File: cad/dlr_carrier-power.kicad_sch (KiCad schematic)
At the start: 25 parts, among them J1 PV_IN, J2 BQ24650, J4 LMR33630ADDA, U1 AP2112K-3.3, U2 LP5907MFX-3.8

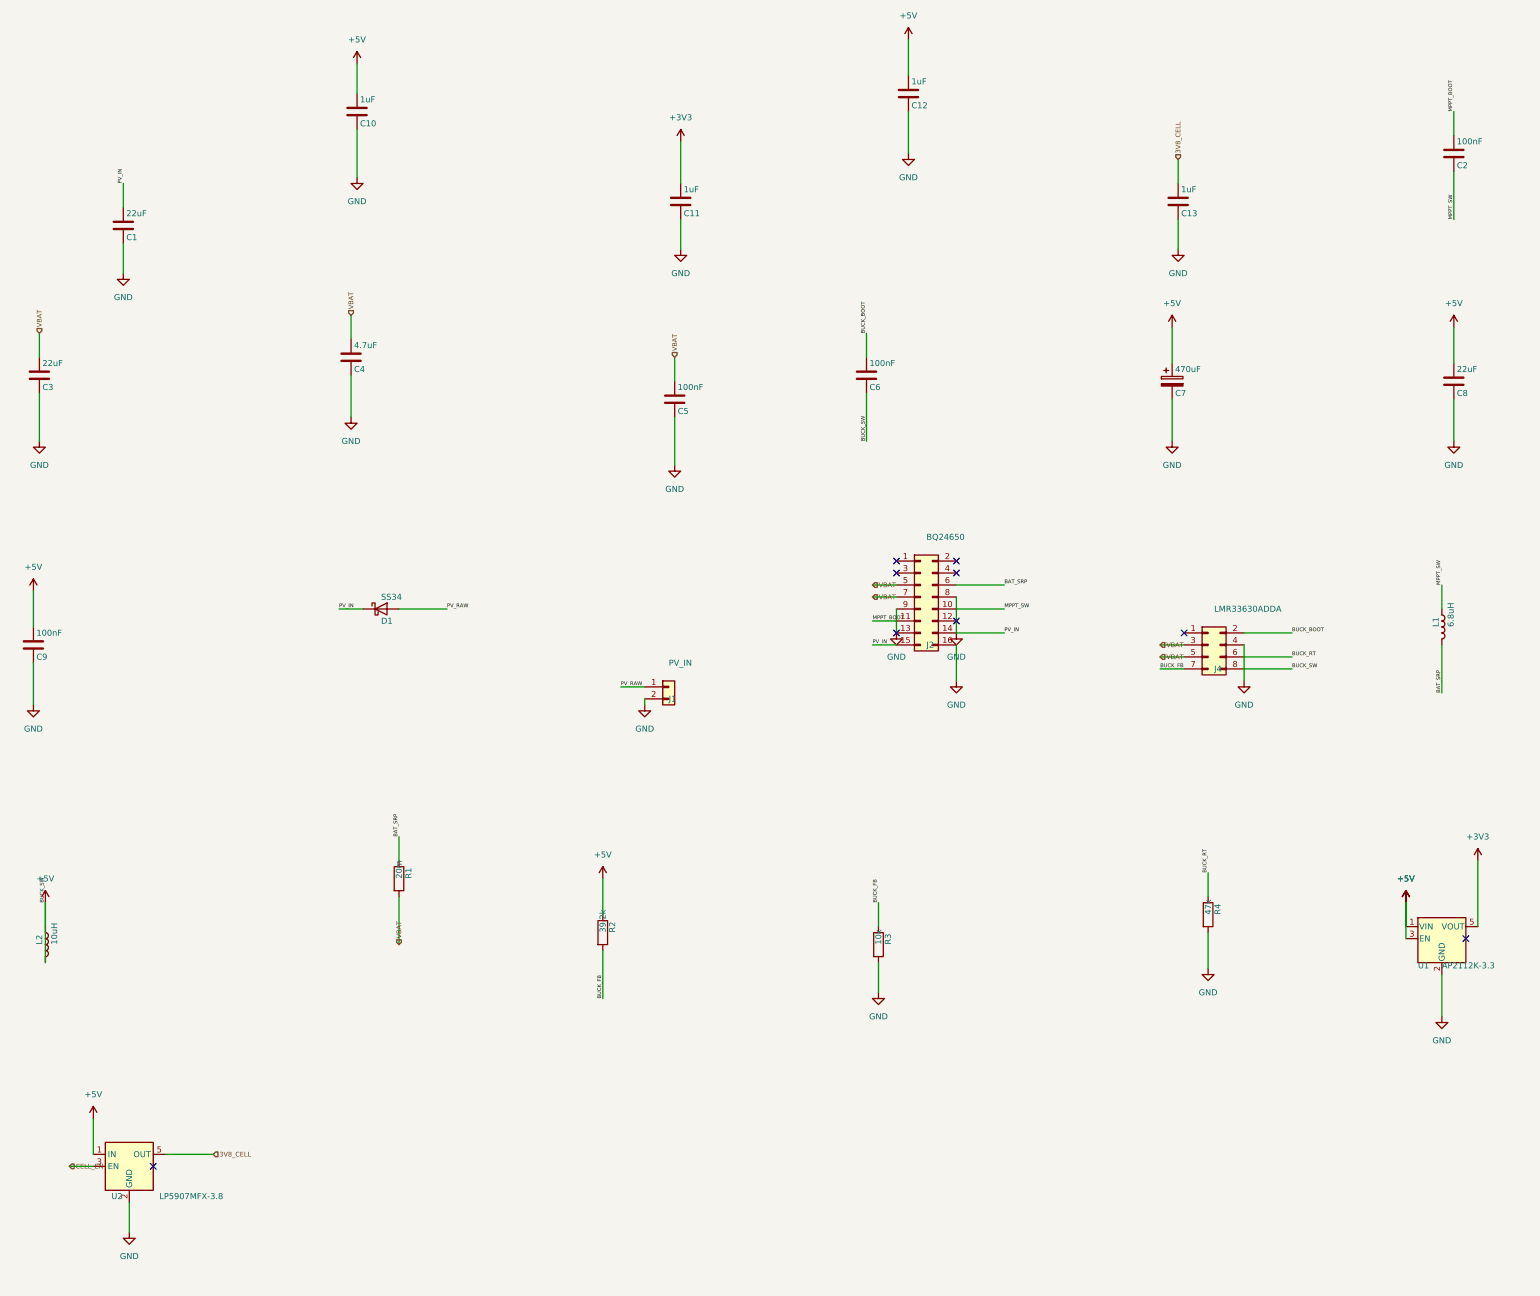
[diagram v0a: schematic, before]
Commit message: 🎨 style: lint fixes (f-string, unused imports, complexity, naming)
CI lint surface from the prior commit:
* F541: drop extraneous `f` prefixes on f-strings without placeholders
* F401: remove unused `math` and `_place_pwr_flags` imports
* C901: extract `_route_sheet_nets` helper so `build_child_sheet`
  complexity drops back under the McCabe threshold
* N806: lowercase local constants in `build_root_sheet`
* black: reformat multi_sheet.py + schematic.py

Co-Authored-By: Claude Opus 4.7 (1M context) <noreply@anthropic.com>
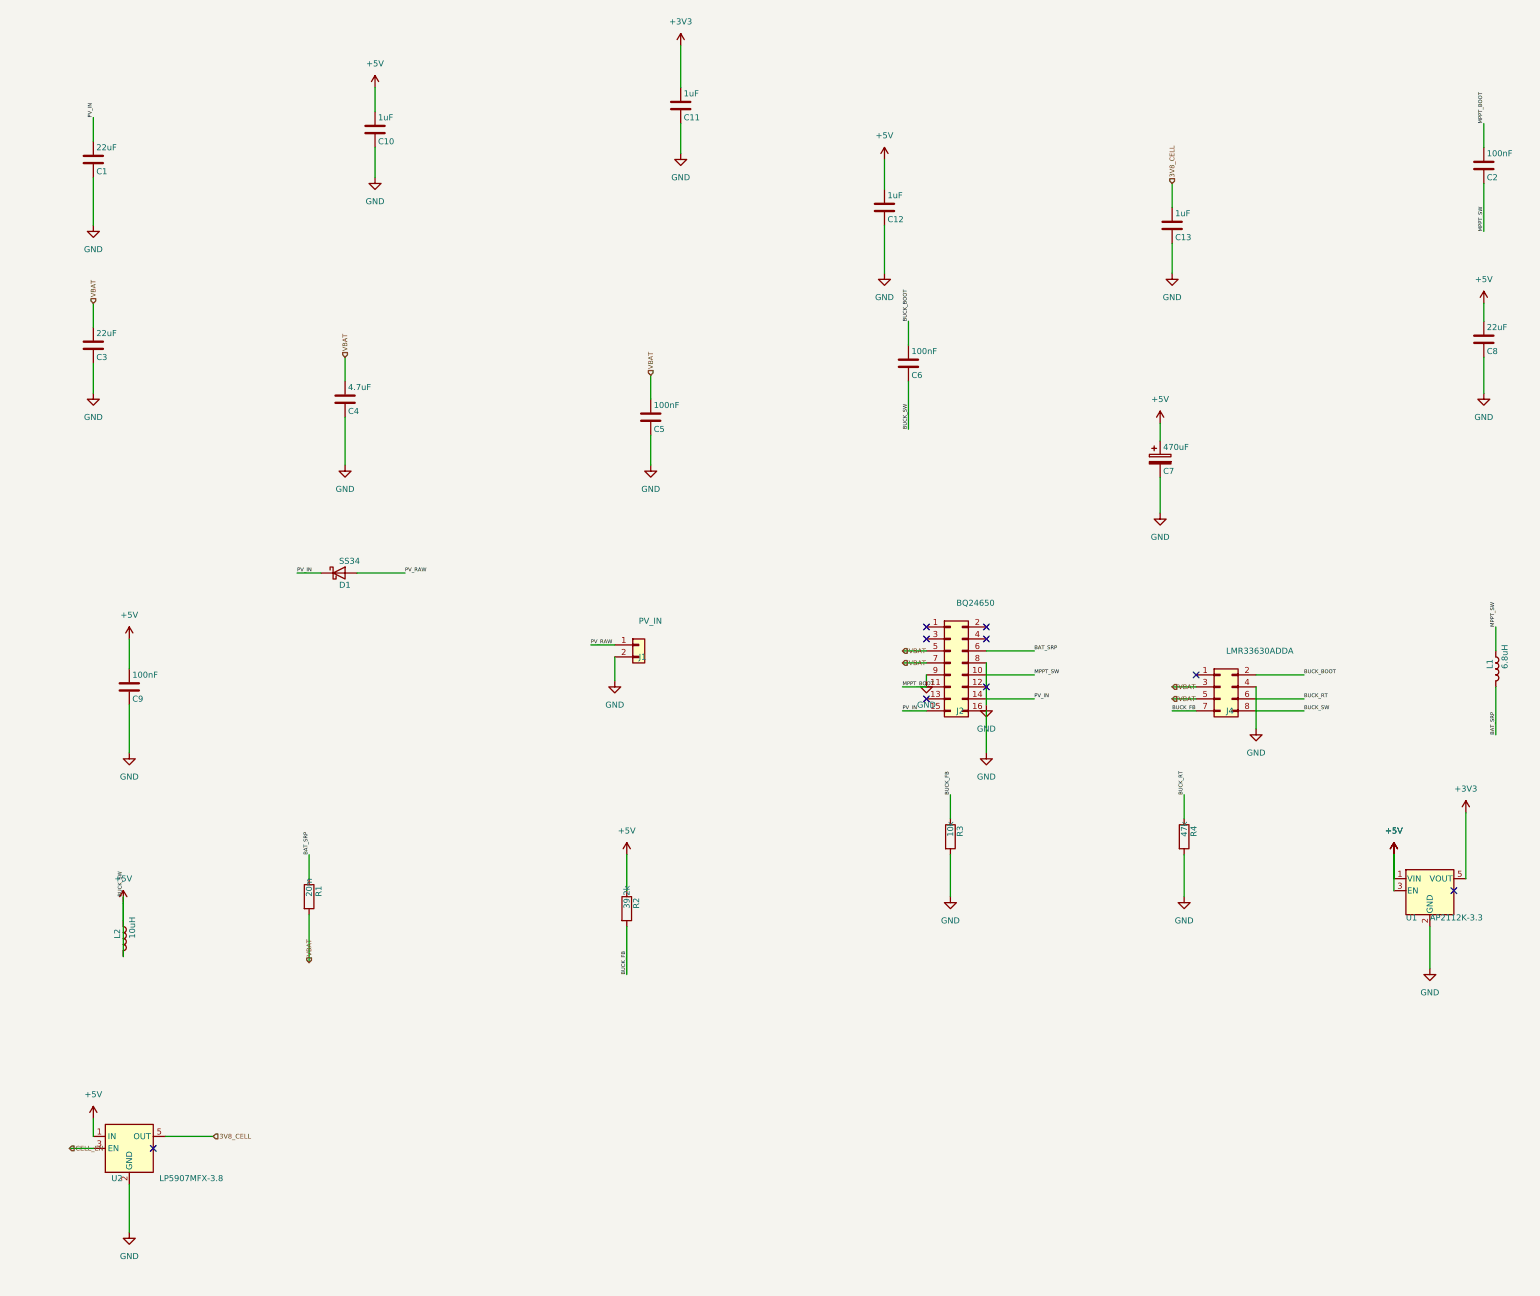
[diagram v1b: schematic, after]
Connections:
- net GND: no longer C1.1, D1.1 (K), J2.13 (Pin_13), J2.14 (Pin_14), J2.15 (Pin_15)
- new net PV_IN: C1.1, D1.1 (K), J2.14 (Pin_14), J2.15 (Pin_15)

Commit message: 🪪 feat(anemometer): low-wind variant — Vaisala WMT702, kit SKU split
Locks the low-wind variant per the grill-me design tree. Single PCB +
single firmware binary; the variant lives in the kit BOM (sensor + cable
harness + PV panel + battery). Both sensors speak NMEA 0183 over the
RS-485 transceiver so the driver is talker-agnostic.

Hardware:
* anemometer.py: add SMBJ24CA TVS on V+→GND for IEC 61000-4-5 2 kV
  surge tolerance (utility-tower deployment).

Theory:
* theory.ipynb §6: variant-aware power-budget cell. WMT702's 480 mW
  draw needs a 30 W panel + 100 Wh battery to hold 1.66× winter margin
  and 2.22 d autonomy. High-wind kit (Calypso, 1 mW) stays on the
  existing 20 W / 50 Wh baseline.
* Expected-values table rebuilt with per-variant rows.

README:
* New "Anemometer Variants" section: full kit BOM table, deployment
  decision rule (NREL WIND Toolkit climatology, 15 % yr V_w<1 m/s
  threshold), fallback policy, per-variant power numbers.

Co-Authored-By: Claude Opus 4.7 (1M context) <noreply@anthropic.com>
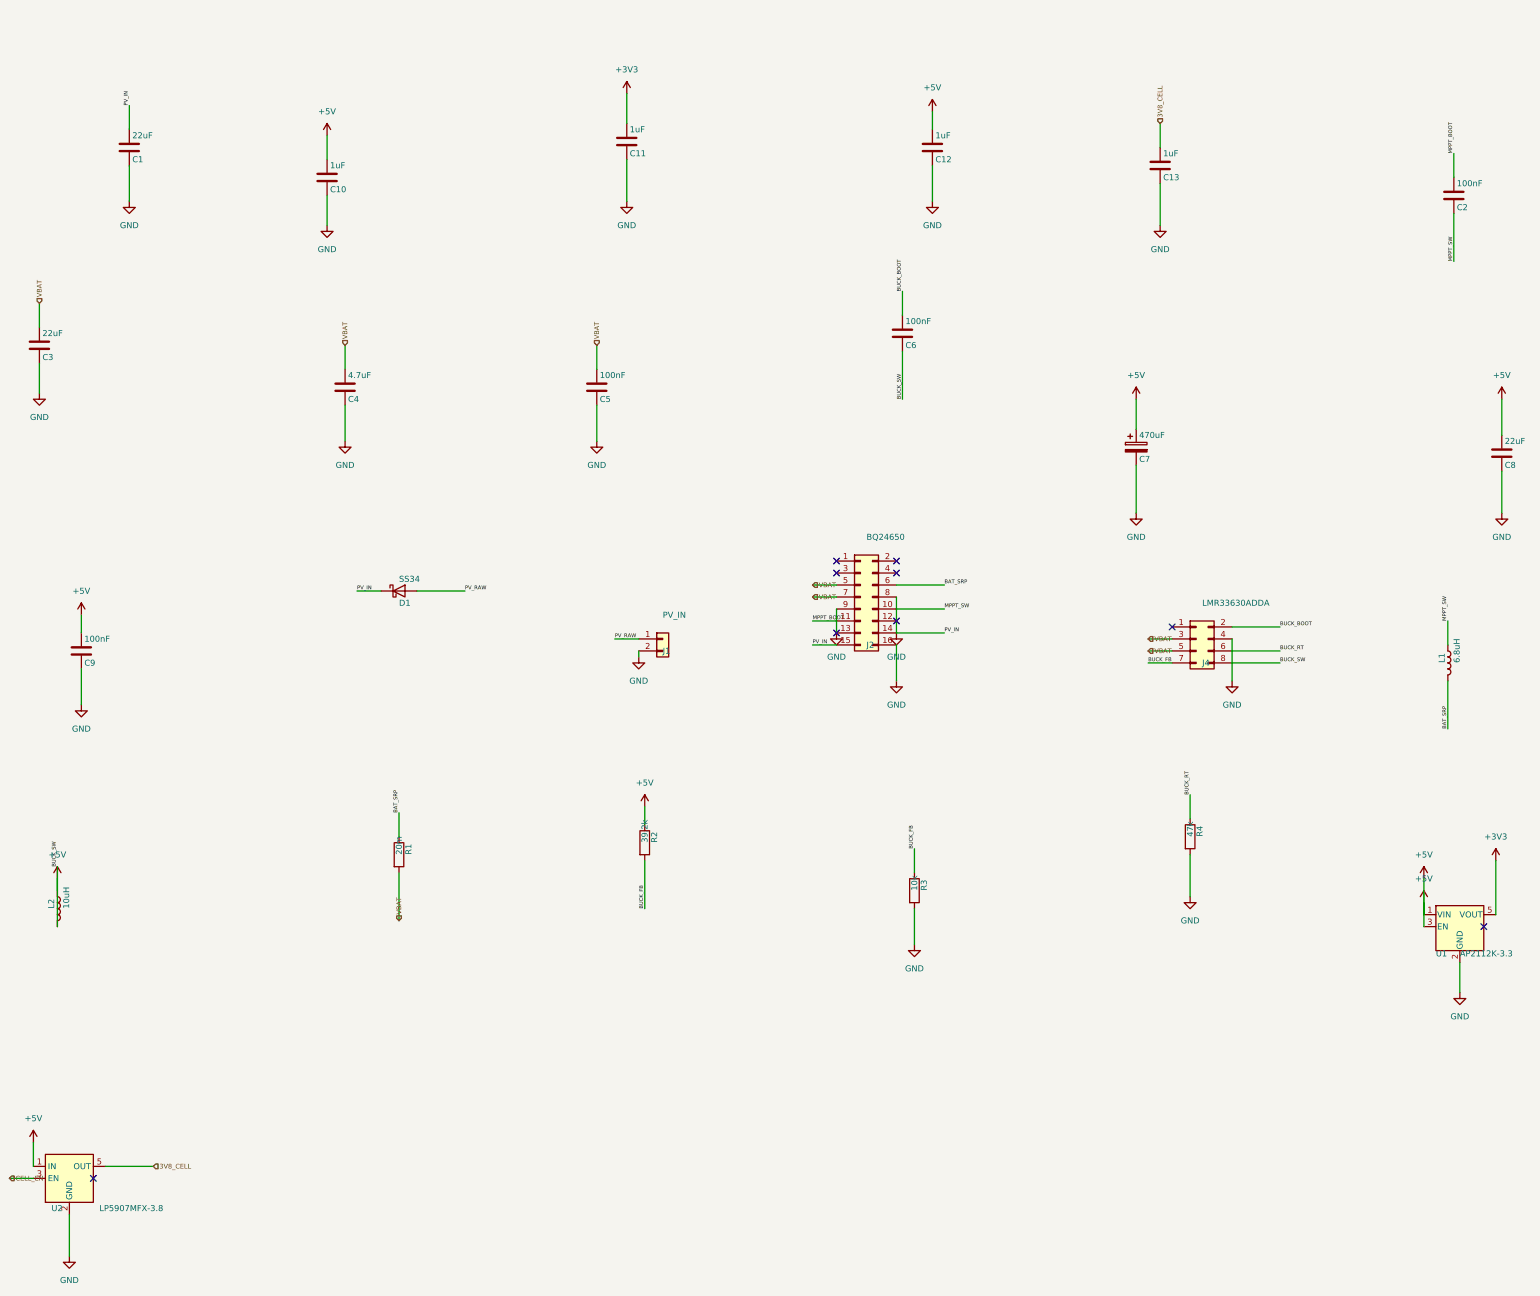
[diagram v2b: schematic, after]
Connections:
- net PV_IN is gone; now on net GND: C1.1, D1.1 (K), J2.14 (Pin_14), J2.15 (Pin_15)
- net GND: now also J2.13 (Pin_13)
